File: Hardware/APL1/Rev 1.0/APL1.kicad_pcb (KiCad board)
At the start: 2 copper layers, 150 x 100 mm, 51 parts, among them J1 6502 BUS, J2 KEYBOARD, J3 SERIAL (DTE), J4 5V DC, J5 PS/2, J6 VIDEO, SW1 POWER, U1 74LS04, U10 ATmega1284-P, U2 6502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

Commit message: Change KBDCLRB to KBDCLR (active high)
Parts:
- added R9: 10k, Resistor_THT:R_Axial_DIN0207_L6.3mm_D2.5mm_P10.16mm_Horizontal, F.Cu at (189.8, 96.3)
- turned C4 to 90 degrees
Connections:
- net KBDCLRB renamed KBDCLR
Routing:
- net KBDCLR: track 36.2 -> 78.1 mm, vias 3 -> 5
- net GND: vias 46 -> 47

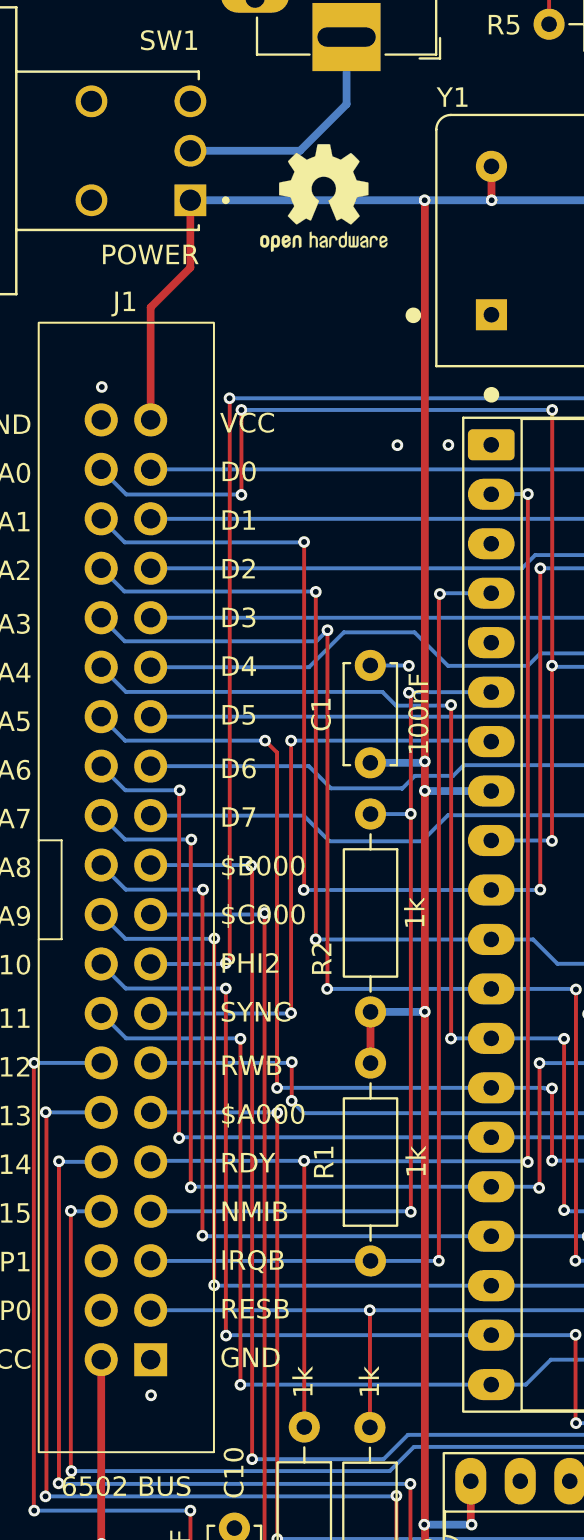
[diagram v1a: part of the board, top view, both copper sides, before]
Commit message: Fix silkscreen and add bulk capacitance
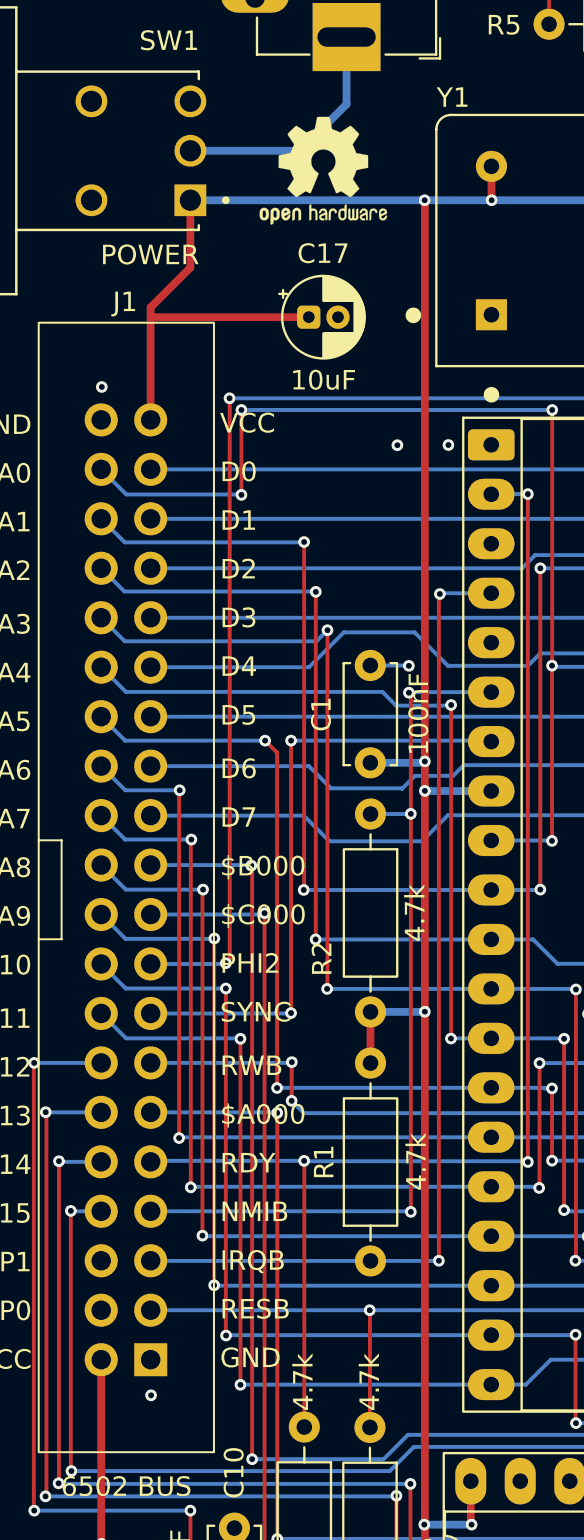
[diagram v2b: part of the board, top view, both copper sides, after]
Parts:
- added C17: 10uF, Capacitor_THT:CP_Radial_D4.0mm_P1.50mm, F.Cu at (69.1, 78.5)
- R1, R2, R3, R4: value 1k -> 4.7k
- moved REF** 1.40 mm to (69.8, 71.0)
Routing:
- net VCC: track 559.2 -> 567.3 mm
